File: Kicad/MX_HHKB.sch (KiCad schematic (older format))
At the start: 136 parts, among them J1 USB_mini_micro_B, K1 Esc, K10 9, K11 0, K12 -, K13 =, K14 Tab, K15 Q, K16 W, K17 E, K18 R, K19 T, K2 1, K20 Y, K21 U, K22 I, K23 O, K24 P, K25 [, K26 ], K27 Ctrl, K28 A, K29 S, K3 2, K30 D, K31 F, K32 G, K33 H, K34 J, K35 K, K36 L, K37 ;, K38 ', K39 Enter, K4 3, K40 L_Shift, K41 Z, K42 X, K43 C, K44 V, K45 B, K46 N, K47 M, K48 ,, K49 ., K5 4, K50 /, K51 R_Shift, K52 Fn, K53 L_GUI, K54 L_ALT, K55 SPACE, K56 R_ALT, K57 R_GUI, K58 \\, K59 `, K6 5, K60 BACKSPACE, K7 6, K8 7, K9 8, SW1 SW_PUSH, U0 ATMEGA32U4, X1 XTAL_GND

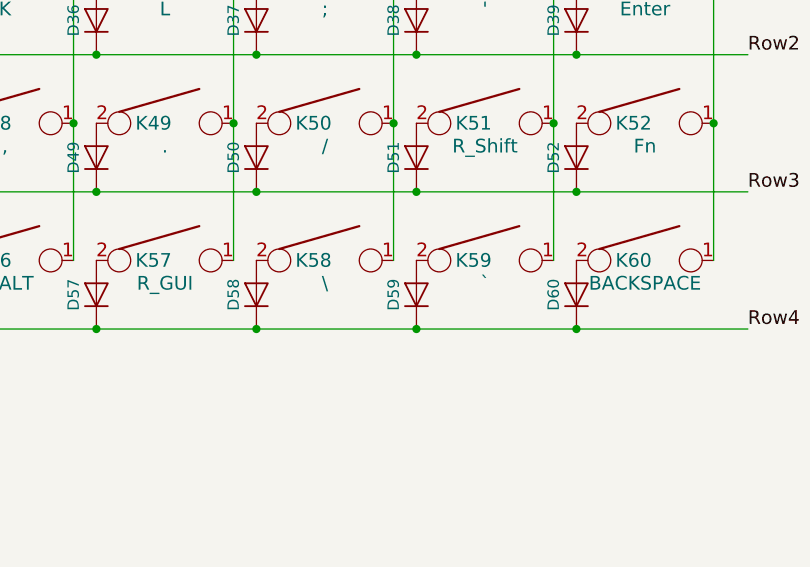
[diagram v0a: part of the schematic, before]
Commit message: - Updated position of Atmega and Crystal - Added render view
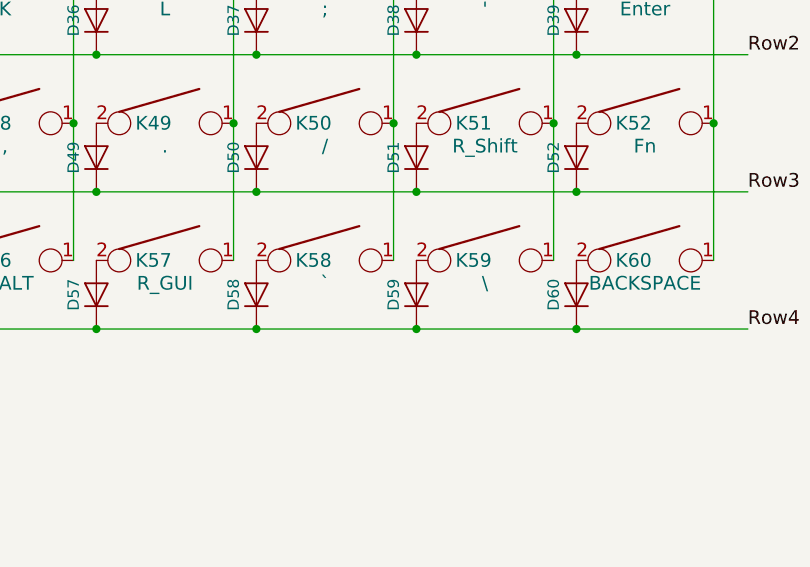
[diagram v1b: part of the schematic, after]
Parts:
- K58: value \\ -> `
- K59: value ` -> \\
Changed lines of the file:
@@
 P 8050 3500
 F 0 "K58" H 8000 3500 60  0000 C CNN
-F 1 "\\" H 8050 3400 60  0000 C CNN
+F 1 "`" H 8050 3400 60  0000 C CNN
 F 2 "Fooprints:Mx_Alps_100" H 8050 3500 60  0001 C CNN
 F 3 "" H 8050 3500 60  0000 C CNN
@@
 P 8750 3500
 F 0 "K59" H 8700 3500 60  0000 C CNN
-F 1 "`" H 8750 3400 60  0000 C CNN
+F 1 "\\" H 8750 3400 60  0000 C CNN
 F 2 "Fooprints:Mx_Alps_100" H 8750 3500 60  0001 C CNN
 F 3 "" H 8750 3500 60  0000 C CNN

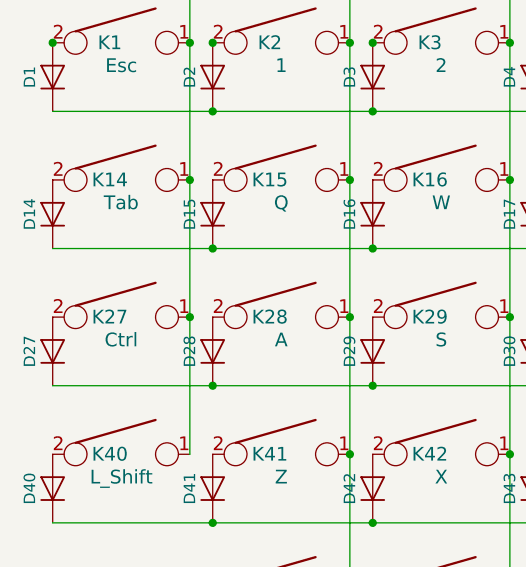
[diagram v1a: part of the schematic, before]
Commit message: - Added 175 stepped Ctrontrol key
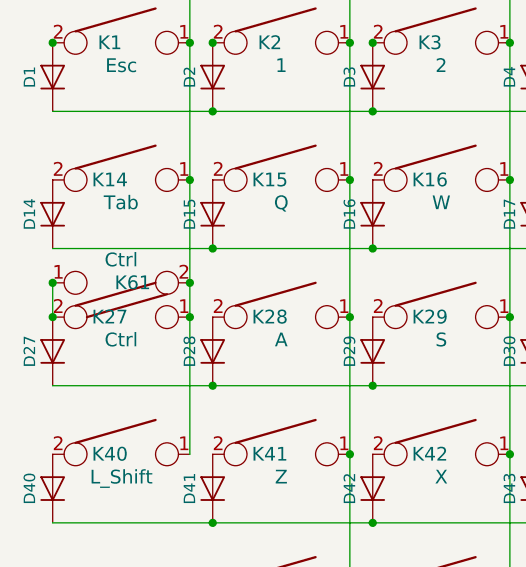
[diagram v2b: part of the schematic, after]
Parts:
- added K61: Ctrl, Footprint:Mx_Alps_175_STEPPED, symbol KEYSW
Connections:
- net Col0: now also K61.2
- net at D27.2 (A), K27.2: now also K61.1
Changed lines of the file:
@@
 Wire Wire Line
 	3000 6550 2000 6550
+$Comp
+L KEYSW K61
+U 1 1 59062EBC
+P 1050 2150
+F 0 "K61" H 1000 2150 60  0000 C CNN
+F 1 "Ctrl" H 1050 2050 60  0000 C CNN
+F 2 "Footprint:Mx_Alps_175_STEPPED" H 1050 2150 60  0001 C CNN
+F 3 "" H 1050 2150 60  0000 C CNN
+	1    1050 2150
+	-1   0    0    1
+$EndComp
+Wire Wire Line
+	750  2150 750  2300
+Connection ~ 750  2300
+Connection ~ 750  2150
+Connection ~ 1350 2150
 $EndSCHEMATC

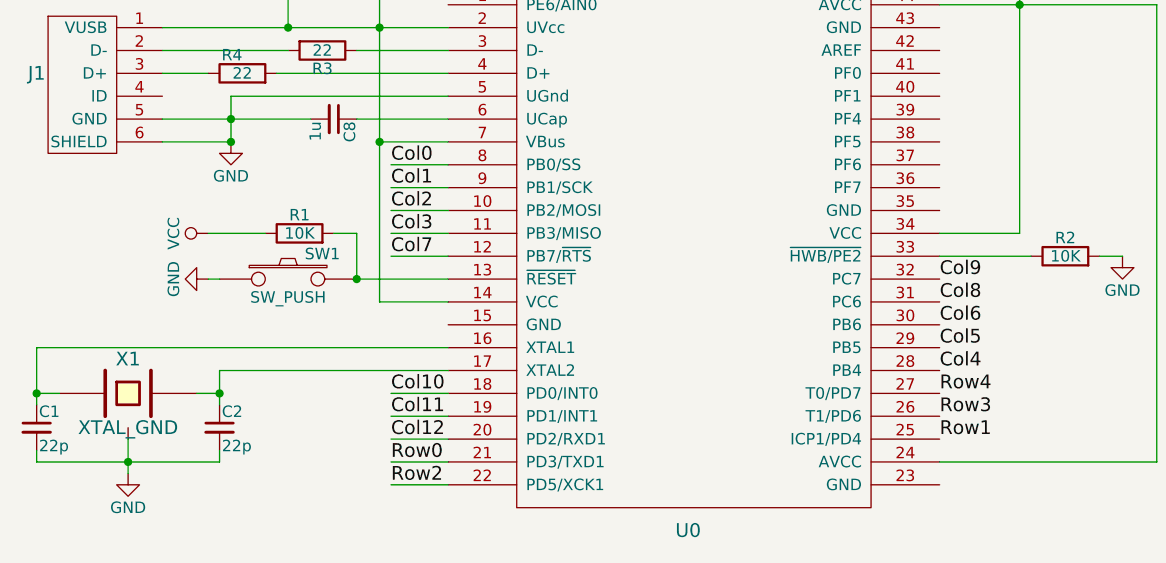
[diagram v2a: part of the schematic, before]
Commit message: - Added darkou and open hardware logo - Updated col/row assignation (simplifying rooting)
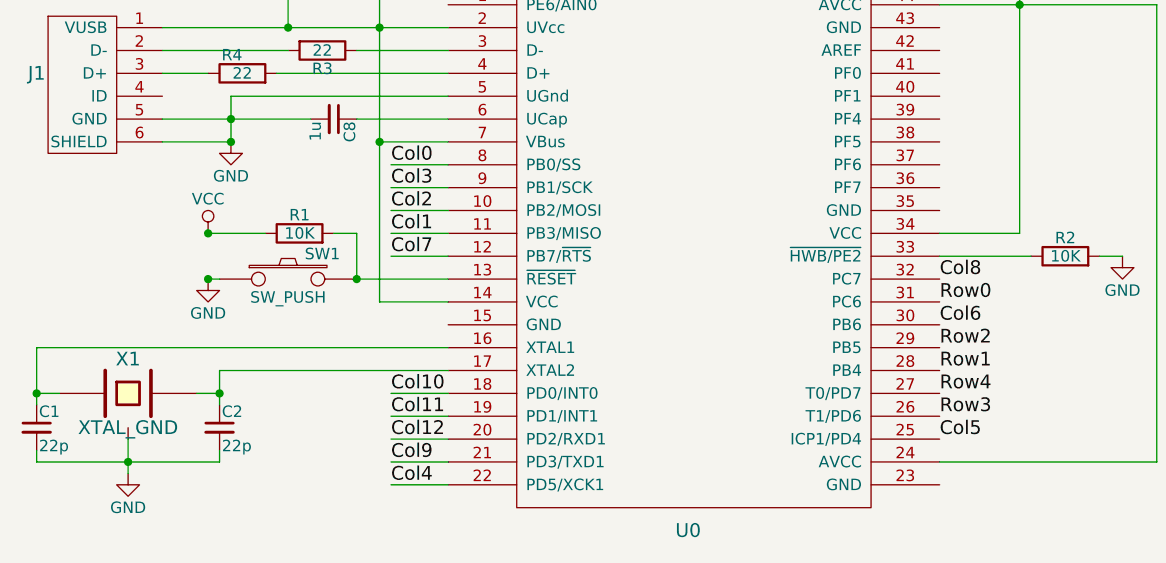
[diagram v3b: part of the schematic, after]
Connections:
- net Col1: now also U0.11 (PB3/MISO); no longer U0.9 (PB1/SCK)
- net Col3: now also U0.9 (PB1/SCK); no longer U0.11 (PB3/MISO)
- net Col4: now also U0.22 (PD5/XCK1); no longer U0.28 (PB4)
- net Col5: now also U0.25 (ICP1/PD4); no longer U0.29 (PB5)
- net Col8: now also U0.32 (PC7); no longer U0.31 (PC6)
- net Col9: now also U0.21 (PD3/TXD1); no longer U0.32 (PC7)
- net Row0: now also U0.31 (PC6); no longer U0.21 (PD3/TXD1)
- net Row1: now also U0.28 (PB4); no longer U0.25 (ICP1/PD4)
- net Row2: now also U0.29 (PB5); no longer U0.22 (PD5/XCK1)
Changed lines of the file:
@@
 F 3 "" H 1950 5950 50  0001 C CNN
 	1    1950 5950
-	0    -1   -1   0
+	1    0    0    -1
 $EndComp
 $Comp
@@
 F 3 "" H 1950 6150 50  0001 C CNN
 	1    1950 6150
-	0    1    1    0
+	1    0    0    -1
 $EndComp
 $Comp
@@
 Text Label 9750 850  0    60   ~ 0
 Col12
-Text Label 2750 5750 0    60   ~ 0
+Text Label 2750 5950 0    60   ~ 0
 Col1
 Text Label 2750 5850 0    60   ~ 0
 Col2
-Text Label 2750 5950 0    60   ~ 0
+Text Label 2750 5750 0    60   ~ 0
 Col3
-Text Label 5150 6550 0    60   ~ 0
+Text Label 2750 7050 0    60   ~ 0
 Col4
-Text Label 5150 6450 0    60   ~ 0
+Text Label 5150 6850 0    60   ~ 0
 Col5
 Text Label 5150 6350 0    60   ~ 0
@@
 Text Label 2750 6050 0    60   ~ 0
 Col7
-Text Label 5150 6250 0    60   ~ 0
+Text Label 5150 6150 0    60   ~ 0
 Col8
-Text Label 5150 6150 0    60   ~ 0
+Text Label 2750 6950 0    60   ~ 0
 Col9
 Text Label 2750 6650 0    60   ~ 0
@@
 Text Label 9900 3800 0    60   ~ 0
 Row4
-Text Label 2750 6950 0    60   ~ 0
+Text Label 5150 6250 0    60   ~ 0
 Row0
-Text Label 5150 6850 0    60   ~ 0
+Text Label 5150 6550 0    60   ~ 0
 Row1
-Text Label 2750 7050 0    60   ~ 0
+Text Label 5150 6450 0    60   ~ 0
 Row2
 Text Label 5150 6750 0    60   ~ 0
@@
 Connection ~ 750  2150
 Connection ~ 1350 2150
+Connection ~ 1950 5950
+Connection ~ 1950 6150
 $EndSCHEMATC

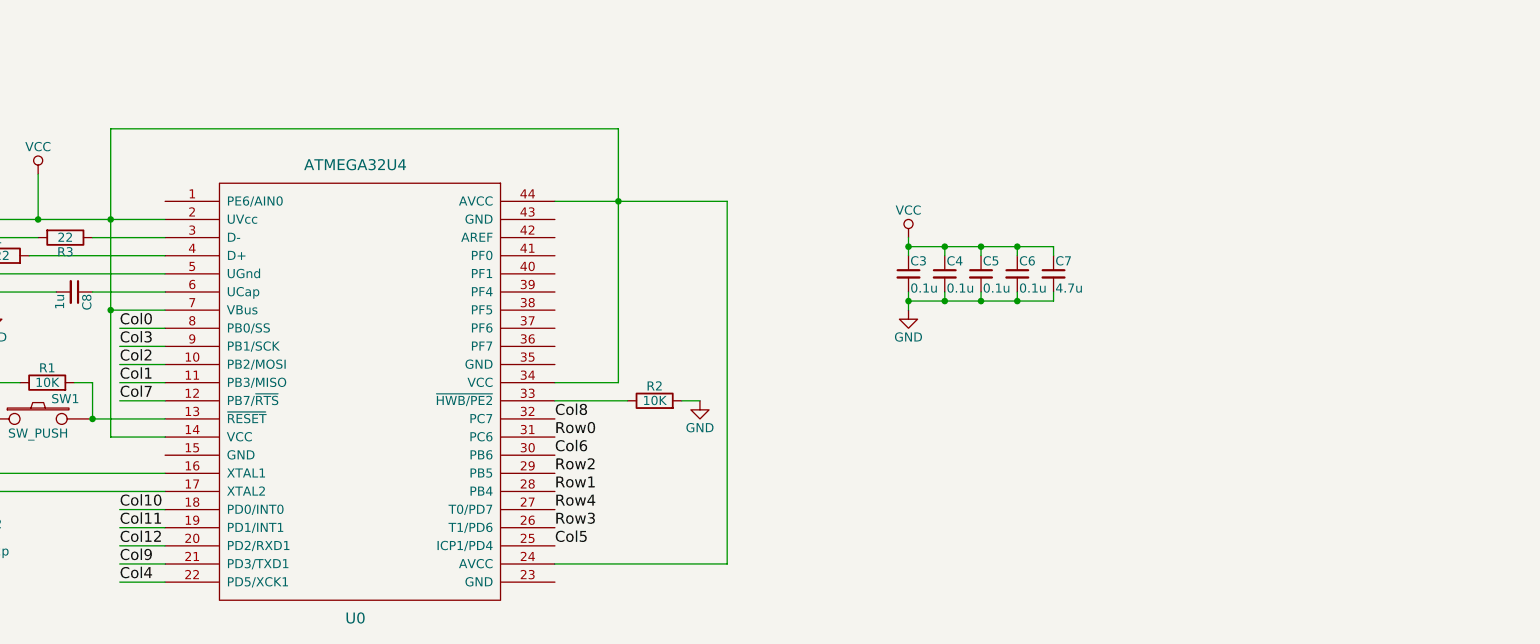
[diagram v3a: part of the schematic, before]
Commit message: - Rerouting some wires - Added led on Esc and Caps locks switches
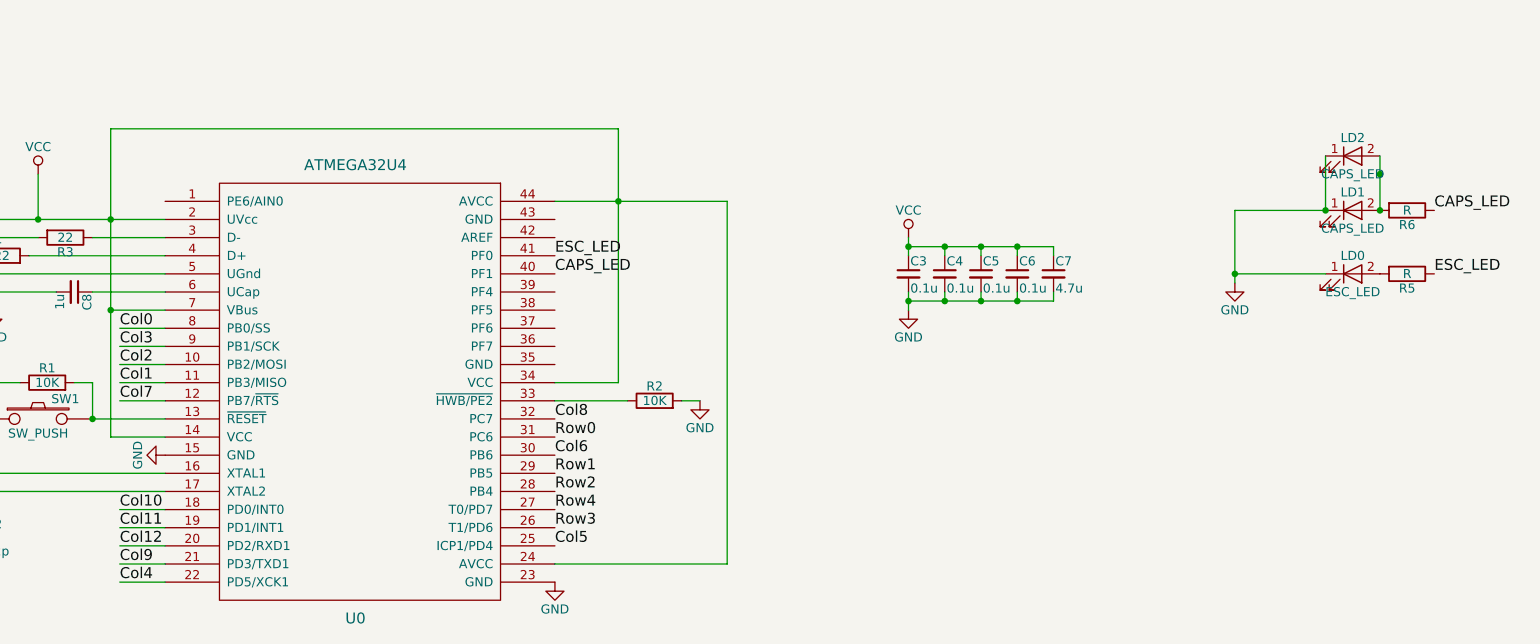
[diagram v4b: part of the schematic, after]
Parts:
- added LD0: ESC_LED, LEDs:LED_D3.0mm, symbol LED
- added LD1, LD2: CAPS_LED, LEDs:LED_D3.0mm, symbol LED
- added R5, R6: R, Resistors_SMD:R_0805_HandSoldering, symbol R
- X1: footprint Crystals:Crystal_SMD_SeikoEpson_TSX3225-4pin_3.2x2.5mm_HandSoldering -> Footprint:FA-238
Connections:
- net GND: now also U0.15 (GND), U0.23 (GND), LD0.1 (K), LD1.1 (K), LD2.1 (K)
- net Row1: now also U0.29 (PB5); no longer U0.28 (PB4)
- net Row2: now also U0.28 (PB4); no longer U0.29 (PB5)
- net CAPS_LED: now reaches U0.40 (PF1)
- net CAPS_LED: now also R6.1
- net ESC_LED: now reaches U0.41 (PF0)
- net ESC_LED: now also R5.1
- new net: LD0.2 (A), R5.2
- new net: LD1.2 (A), LD2.2 (A), R6.2
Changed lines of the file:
@@
 F 0 "X1" H 1600 6800 60  0000 C CNN
 F 1 "XTAL_GND" H 1600 6500 60  0000 C CNN
-F 2 "Crystals:Crystal_SMD_SeikoEpson_TSX3225-4pin_3.2x2.5mm_HandSoldering" H 1600 6650 60  0001 C CNN
+F 2 "Footprint:FA-238" H 1600 6650 60  0001 C CNN
 F 3 "" H 1600 6650 60  0000 C CNN
 	1    1600 6650
@@
 Text Label 5150 6250 0    60   ~ 0
 Row0
+Text Label 5150 6450 0    60   ~ 0
+Row1
 Text Label 5150 6550 0    60   ~ 0
-Row1
-Text Label 5150 6450 0    60   ~ 0
 Row2
 Text Label 5150 6750 0    60   ~ 0
@@
 Connection ~ 2700 5050
 Wire Wire Line
-	5150 5950 5500 5950
-Wire Wire Line
-	5500 5950 5500 4550
+	5500 5950 5150 5950
+Wire Wire Line
+	5500 4550 5500 5950
 Wire Wire Line
 	5500 4550 2700 4550
@@
 Connection ~ 1950 5950
 Connection ~ 1950 6150
+$Comp
+L LED LD0
+U 1 1 59075987
+P 9550 5350
+F 0 "LD0" H 9550 5450 50  0000 C CNN
+F 1 "ESC_LED" H 9550 5250 50  0000 C CNN
+F 2 "LEDs:LED_D3.0mm" H 9550 5350 50  0001 C CNN
+F 3 "" H 9550 5350 50  0001 C CNN
+	1    9550 5350
+	1    0    0    -1
+$EndComp
+$Comp
+L R R5
+U 1 1 59075E70
+P 9850 5350
+F 0 "R5" V 9930 5350 50  0000 C CNN
+F 1 "R" V 9850 5350 50  0000 C CNN
+F 2 "Resistors_SMD:R_0805_HandSoldering" V 9780 5350 50  0001 C CNN
+F 3 "" H 9850 5350 50  0001 C CNN
+	1    9850 5350
+	0    1    1    0
+$EndComp
+$Comp
+L GND #PWR09
+U 1 1 59076AE3
+P 8900 5400
+F 0 "#PWR09" H 8900 5150 50  0001 C CNN
+F 1 "GND" H 8900 5250 50  0000 C CNN
+F 2 "" H 8900 5400 50  0001 C CNN
+F 3 "" H 8900 5400 50  0001 C CNN
+	1    8900 5400
+	1    0    0    -1
+$EndComp
+Wire Wire Line
+	9400 5350 8900 5350
+Wire Wire Line
+	8900 5000 8900 5400
+$Comp
+L LED LD1
+U 1 1 5907938D
+P 9550 5000
+F 0 "LD1" H 9550 5100 50  0000 C CNN
+F 1 "CAPS_LED" H 9550 4900 50  0000 C CNN
+F 2 "LEDs:LED_D3.0mm" H 9550 5000 50  0001 C CNN
+F 3 "" H 9550 5000 50  0001 C CNN
+	1    9550 5000
+	1    0    0    -1
+$EndComp
+$Comp
+L R R6
+U 1 1 59079393
+P 9850 5000
+F 0 "R6" V 9930 5000 50  0000 C CNN
+F 1 "R" V 9850 5000 50  0000 C CNN
+F 2 "Resistors_SMD:R_0805_HandSoldering" V 9780 5000 50  0001 C CNN
+F 3 "" H 9850 5000 50  0001 C CNN
+	1    9850 5000
+	0    1    1    0
+$EndComp
+Wire Wire Line
+	9400 5000 8900 5000
+Connection ~ 8900 5350
+Text Label 10000 5000 0    60   ~ 0
+CAPS_LED
+Text Label 10000 5350 0    60   ~ 0
+ESC_LED
+Text Label 5150 5250 0    60   ~ 0
+ESC_LED
+Text Label 5150 5350 0    60   ~ 0
+CAPS_LED
+$Comp
+L GND #PWR010
+U 1 1 5907C578
+P 5150 7050
+F 0 "#PWR010" H 5150 6800 50  0001 C CNN
+F 1 "GND" H 5150 6900 50  0000 C CNN
+F 2 "" H 5150 7050 50  0001 C CNN
+F 3 "" H 5150 7050 50  0001 C CNN
+	1    5150 7050
+	1    0    0    -1
+$EndComp
+$Comp
+L GND #PWR011
+U 1 1 5907C72A
+P 3000 6350
+F 0 "#PWR011" H 3000 6100 50  0001 C CNN
+F 1 "GND" H 3000 6200 50  0000 C CNN
+F 2 "" H 3000 6350 50  0001 C CNN
+F 3 "" H 3000 6350 50  0001 C CNN
+	1    3000 6350
+	0    1    1    0
+$EndComp
+$Comp
+L LED LD2
+U 1 1 5907E4EF
+P 9550 4700
+F 0 "LD2" H 9550 4800 50  0000 C CNN
+F 1 "CAPS_LED" H 9550 4600 50  0000 C CNN
+F 2 "LEDs:LED_D3.0mm" H 9550 4700 50  0001 C CNN
+F 3 "" H 9550 4700 50  0001 C CNN
+	1    9550 4700
+	1    0    0    -1
+$EndComp
+Wire Wire Line
+	9400 4700 9400 5000
+Connection ~ 9400 5000
+Connection ~ 9700 4800
+Wire Wire Line
+	9700 4700 9700 5000
+Connection ~ 9700 5000
 $EndSCHEMATC

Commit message: - Some routing updates
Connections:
- net CAPS_LED: now also U0.1 (PE6/AIN0); no longer U0.40 (PF1)
- net Col4: now also U0.21 (PD3/TXD1); no longer U0.22 (PD5/XCK1)
- net Col5: now also U0.22 (PD5/XCK1); no longer U0.25 (ICP1/PD4)
- net Col6: now also U0.29 (PB5); no longer U0.30 (PB6)
- net Col8: now also U0.31 (PC6); no longer U0.32 (PC7)
- net Col9: now also U0.32 (PC7); no longer U0.21 (PD3/TXD1)
- net Row0: now also U0.30 (PB6); no longer U0.31 (PC6)
- net Row1: now also U0.28 (PB4); no longer U0.29 (PB5)
- net Row2: now also U0.27 (T0/PD7); no longer U0.28 (PB4)
- net Row4: now also U0.25 (ICP1/PD4); no longer U0.27 (T0/PD7)
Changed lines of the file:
@@
 Text Label 2750 5750 0    60   ~ 0
 Col3
+Text Label 2750 6950 0    60   ~ 0
+Col4
 Text Label 2750 7050 0    60   ~ 0
-Col4
-Text Label 5150 6850 0    60   ~ 0
 Col5
-Text Label 5150 6350 0    60   ~ 0
+Text Label 5150 6450 0    60   ~ 0
 Col6
 Text Label 2750 6050 0    60   ~ 0
 Col7
+Text Label 5150 6250 0    60   ~ 0
+Col8
 Text Label 5150 6150 0    60   ~ 0
-Col8
-Text Label 2750 6950 0    60   ~ 0
 Col9
 Text Label 2750 6650 0    60   ~ 0
@@
 Text Label 9900 3800 0    60   ~ 0
 Row4
-Text Label 5150 6250 0    60   ~ 0
+Text Label 5150 6350 0    60   ~ 0
 Row0
-Text Label 5150 6450 0    60   ~ 0
+Text Label 5150 6550 0    60   ~ 0
 Row1
-Text Label 5150 6550 0    60   ~ 0
+Text Label 5150 6650 0    60   ~ 0
 Row2
 Text Label 5150 6750 0    60   ~ 0
 Row3
-Text Label 5150 6650 0    60   ~ 0
+Text Label 5150 6850 0    60   ~ 0
 Row4
 $Comp
@@
 Text Label 5150 5250 0    60   ~ 0
 ESC_LED
-Text Label 5150 5350 0    60   ~ 0
+Text Label 3000 4950 0    60   ~ 0
 CAPS_LED
 $Comp
